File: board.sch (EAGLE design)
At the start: 81 parts, among them IC1 LD1117V33, J1 BLIGHT, J10 BATT, J11 LHBEAMOUT, J12 HORHOUT, J13 12V_SUPPLY, J14 STOPOUT, J15 TURNOUT, J16 FANOUT, J17 BLIGHTOUT, J18 AUXOUT, J2 LHBEAM, J20 455-1750-1-ND, J3 LRTURN, J4 WARN, J5 HORN, J6 BREAK, J7 AUX, J8 TEMP, J9 CAN, Q1 PHP20NQ20T, Q2 PHP20NQ20T, Q3 PHP20NQ20T, U1 MC14504BDR2G, U2 MAX3051ESA+T, U3 VOM1271T, U4 VOM1271T, U5 VOM1271T, U6 ACS711KLCTR-12AB-T, U7 ACS711ELCTR-25AB-T

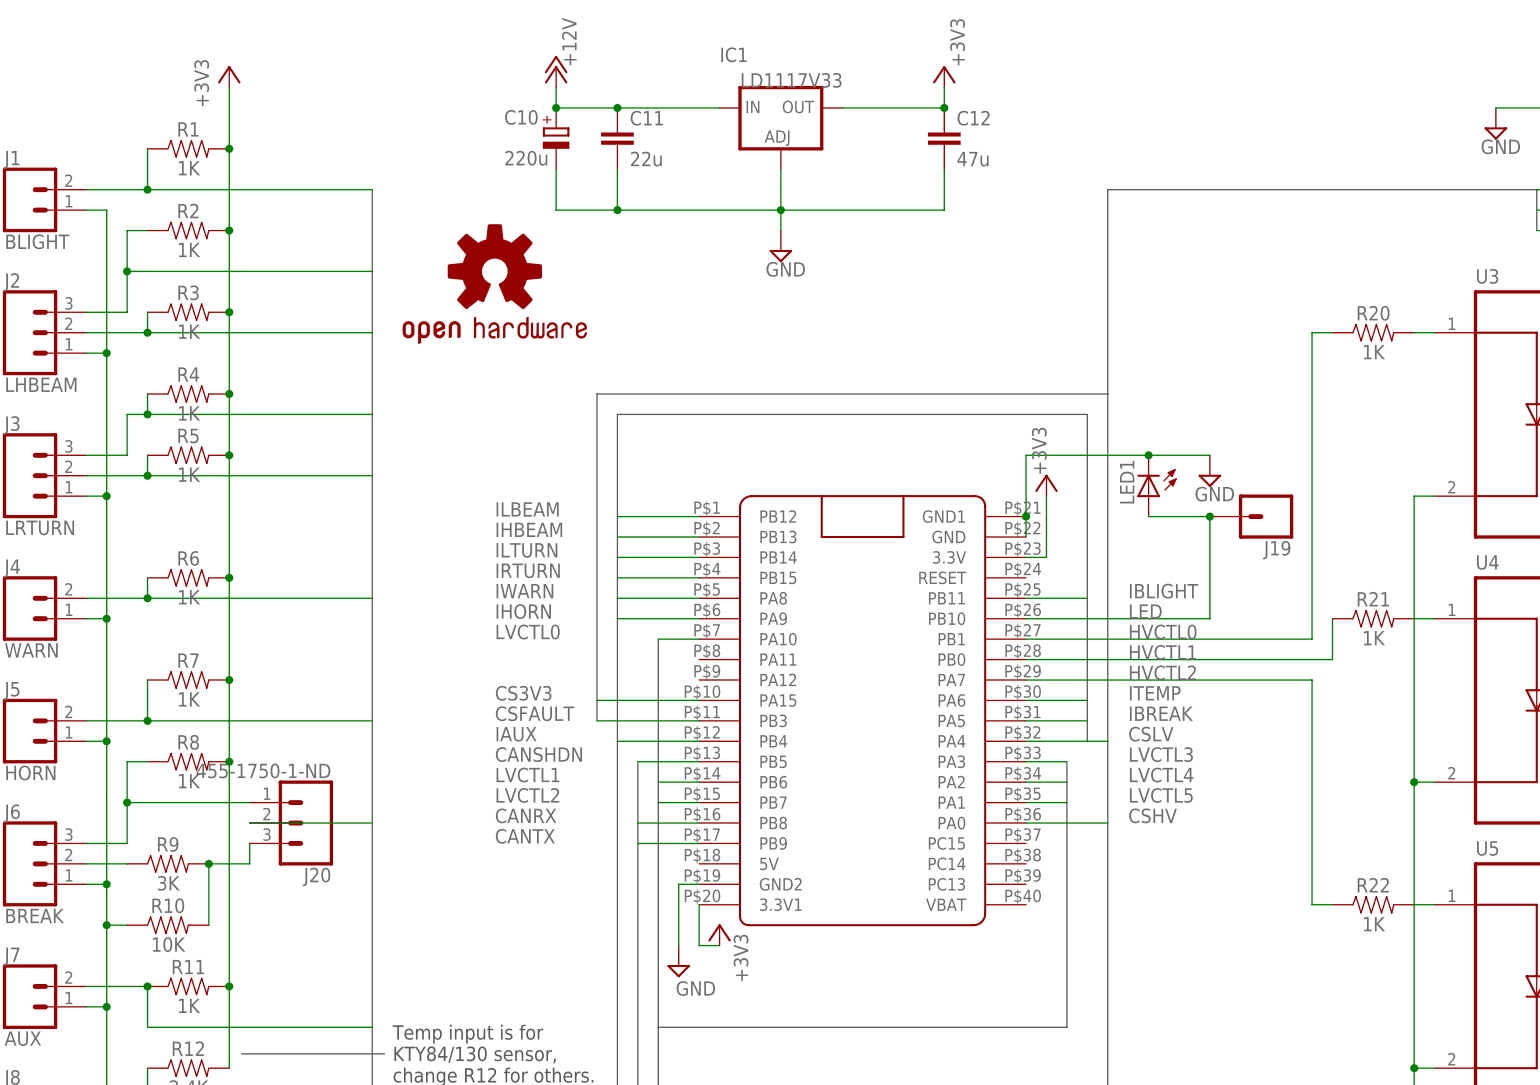
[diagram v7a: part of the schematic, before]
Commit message: BOM for v2
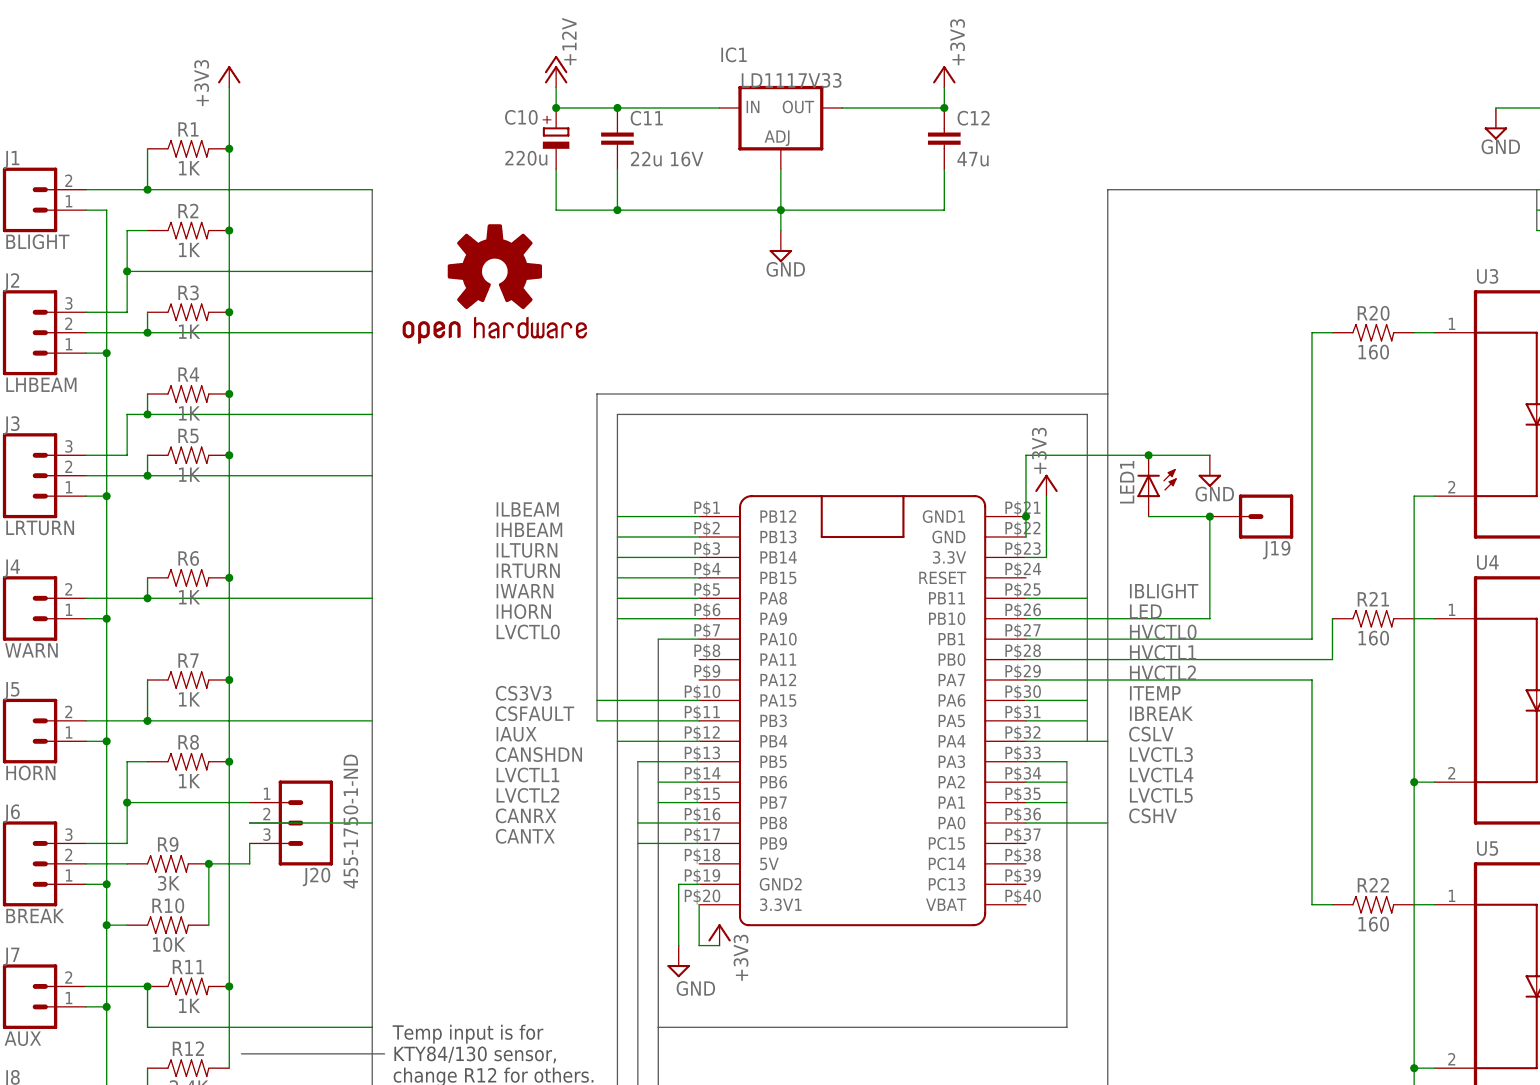
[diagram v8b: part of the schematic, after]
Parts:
- C10: MPN (none) -> SK016M0220BZF-0611
- C11: value 22u -> 22u 16V; MPN (none) -> CL31A226KOHNNNE
- C12: MPN (none) -> CL31A476MQHNNNE
- C9: MPN (none) -> SK016M0470B3F-0811
- J19: MPN (none) -> PLS-1
- J20: MPN (none) -> PLS-3
- JP2: MPN (none) -> PLS-2
- LED1: MPN (none) -> KPT-2012ZGC
- Q4, Q5, Q6, Q7, Q8, Q9: MPN (none) -> IRF7424TRPBF
- R1, R11, R2, R3, R4, R5, R6, R7, R8: MPN (none) -> RC0603JR-071KL
- R10, R14, R15, R16, R17, R18, R19: MPN (none) -> RC0603JR-0710KL
- R12: MPN (none) -> RC0603FR-072K4L
- R13: MPN (none) -> RC0603FR-07120RL
- R20, R21, R22: value 1K -> 160; MPN (none) -> RC0805FR-07160RL
- R9: MPN (none) -> RC0603JR-073KL
- U1: MPN (none) -> MC14504BDR2G
- U2: MPN (none) -> MAX3051ESA+T
- U3, U4, U5: MPN (none) -> VOM1271T
